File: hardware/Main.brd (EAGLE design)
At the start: 86.4 x 49.7 mm, 92 parts, among them IC1 ESP32-WROOM-32D_M113DH3200PH3Q, IC2 LAN8720A-CP-ABC, IC3 R-78E5.0-1.0, IC4 LT1129MPST-3.3#PBF, IC5 74LVT2244PW,118, J2 1727078, J3 HR911105A, J4 1727010, J5 1727049, J6 1727049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

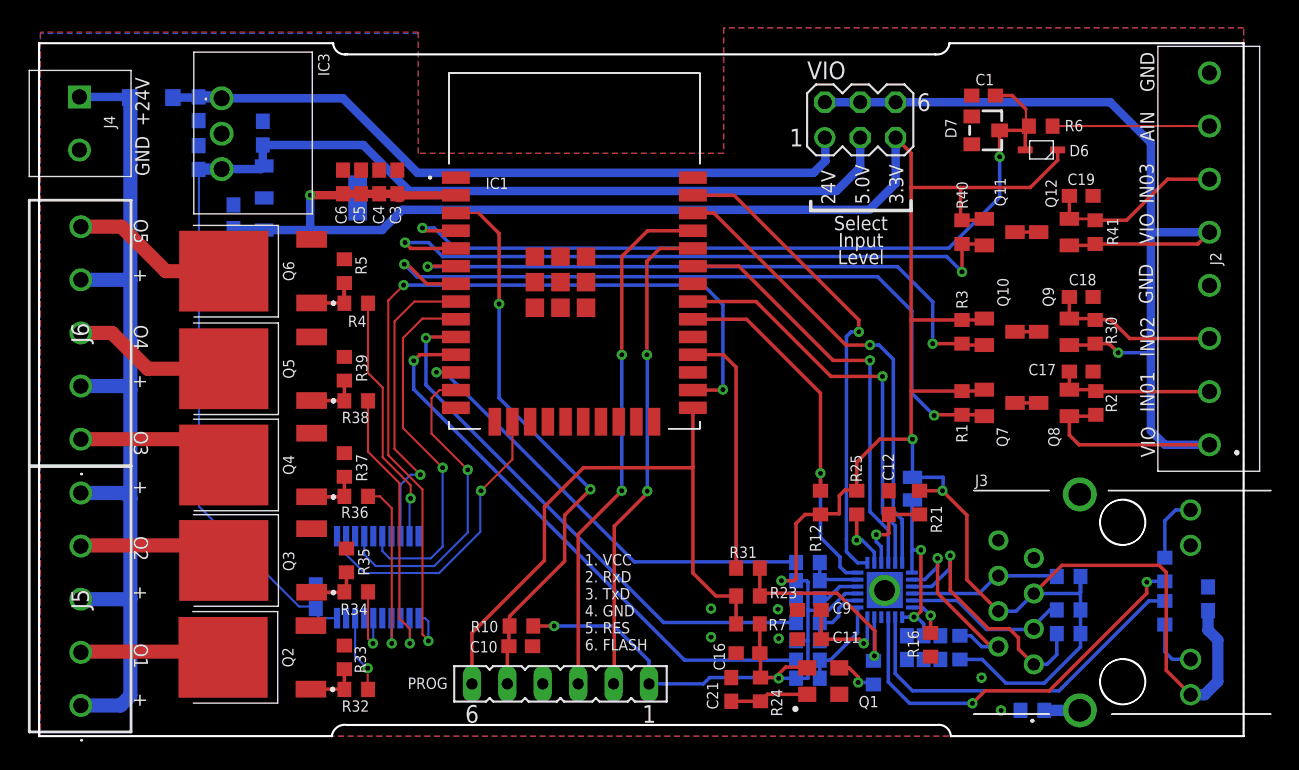
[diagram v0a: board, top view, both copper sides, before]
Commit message: 1-gater ic statt 6 fach Treiber
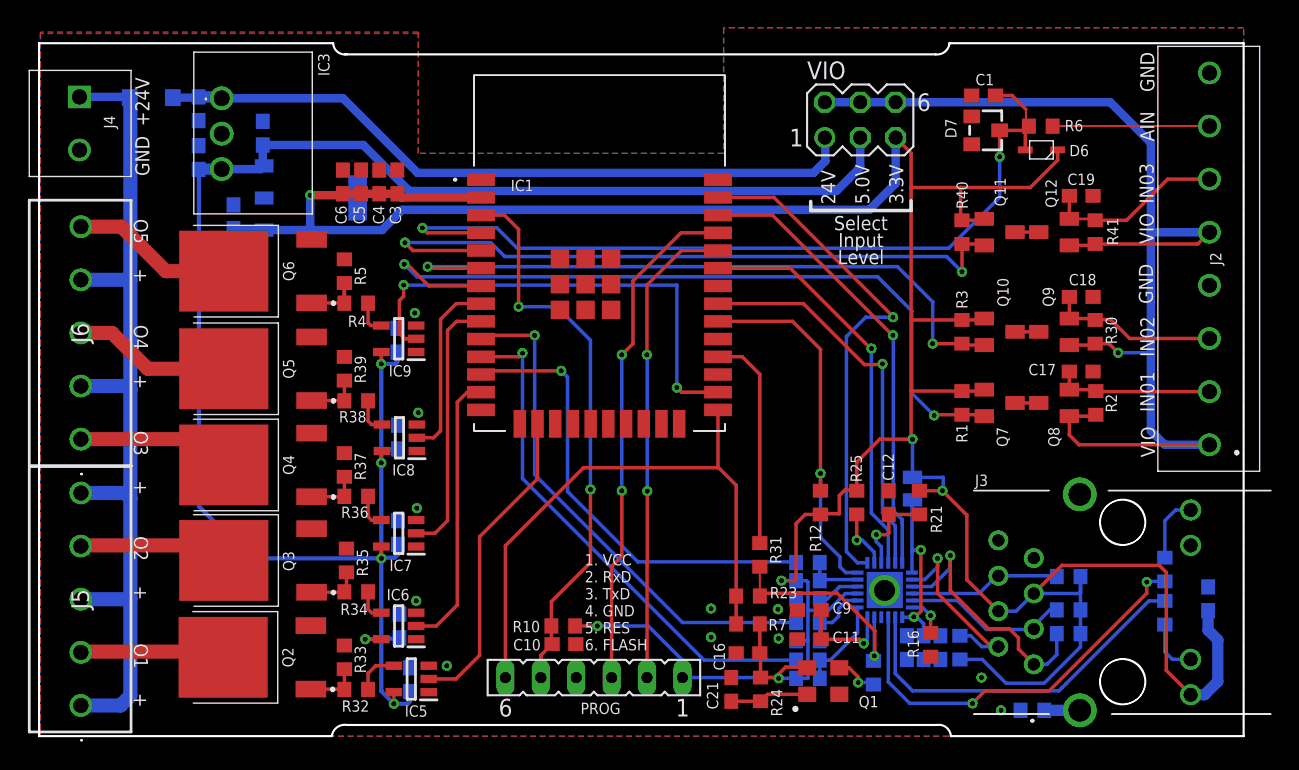
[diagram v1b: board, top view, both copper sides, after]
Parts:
- added C24, C25, C26, C27: 100nF, rcl:C0603
- added IC6, IC7, IC8, IC9: SN74LVC1G17DBVR, SamacSys_Parts:SOT95P280X145-5N
- IC5: value 74LVT2244PW,118 -> SN74LVC1G17DBVR; device SamacSys_Parts:SOP65P640X110-20N -> SamacSys_Parts:SOT95P280X145-5N
- moved IC5 7.68 mm to (26.7, 4.10), flipped to the top, turned to 180 degrees
- moved C23 6.36 mm to (25.9, 7.90)
- moved C10 3.10 mm to (37.6, 6.60)
- moved R10 3.00 mm to (37.6, 7.90)
- moved PROG 2.44 mm to (39.8, 4.20)
- moved IC1 1.81 mm to (40.2, 34.6)
- moved R31 1.27 mm to (51.7, 13.0), turned to 270 degrees
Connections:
- net +5V: now also C24.1, C25.1, C26.1, C27.1, IC5.5, IC6.5, IC7.5, IC8.5, IC9.5; no longer IC5.20
- net GND: now also C24.2, C25.2, C26.2, C27.2, IC5.3, IC6.3, IC7.3, IC8.3, IC9.3; no longer IC5.1, IC5.10, IC5.13, IC5.15, IC5.17, IC5.19
- net N$1: now also IC5.4; no longer IC5.18
- net N$10: now also IC7.4; no longer IC5.14
- net N$17: now also IC8.4; no longer IC5.12
- net N$32: now also IC9.4; no longer IC5.9
- net N$7: now also IC6.4; no longer IC5.16
- net REL_CH_01: now also IC6.2; no longer IC5.4
- net REL_CH_02: now also IC7.2; no longer IC5.6
- net REL_CH_03: now also IC8.2; no longer IC5.8
- net REL_CH_04: now also IC9.2; no longer IC5.11
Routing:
- net +5V: track 91.0 -> 131.2 mm, vias 0 -> 5
- net REL_CH_04: track 61.1 -> 35.0 mm, vias 3 -> 2
- net N$17: track 20.5 -> 2.55 mm, vias 1 -> 0
- net N$32: track 18.0 -> 2.43 mm, vias 1 -> 0
- net N$10: track 13.6 -> 2.50 mm, vias 1 -> 0
- net REL_CH_03: track 22.2 -> 13.3 mm, vias 1 -> 0
- net REL_CH_02: track 26.5 -> 19.0 mm, vias 1 -> 0
- net ETH_RXD1: track 40.7 -> 37.1 mm
- net N$7: track 5.67 -> 2.30 mm, vias 1 -> 0
- net REL_CH_01: track 22.8 -> 20.1 mm, vias 1 -> 0
- net ETH_MDC: track 34.7 -> 37.3 mm
- net N$1: track 5.55 -> 3.26 mm, vias 1 -> 0
- net IO17: track 17.9 -> 15.6 mm
- net ETH_RXD0: track 39.2 -> 37.1 mm
- net INPUT_03: track 48.3 -> 50.1 mm
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
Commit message: ein paar Änderungen in der Beschriftung
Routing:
- net ETH_RXD1: track 37.1 -> 36.4 mm
- net +3V3: track 243.1 -> 242.5 mm
- net ETH_CRS_DV: track 33.2 -> 32.6 mm
- net ETH_RXD0: track 37.1 -> 36.5 mm
